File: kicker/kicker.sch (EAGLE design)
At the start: 21 parts, among them T1 NPN_BC817,215, T3 NPN_BC817,215, X1 JST-XH-06-PIN-LONG-PAD

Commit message: Updating designs
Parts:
- added T2, T4: NPN_BC817,215, rhoban:NPN_BC817,215
- R1: value 1K -> 3K; FARNELL 2446904 -> 2446965
- R4: value 1K -> 3K
- U$1, U$11: FARNELL 1095012 -> 2429705
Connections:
- new net N$5: R1.1, T2.B
- new net N$6: R4.1, T4.B
- net GND: now also T2.E, T4.E
- net KICK1: now also R1.2; no longer R1.1
- net N$1: now also T2.C; no longer R1.2
- net N$3: now also T4.C; no longer R4.1
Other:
- moved on the sheet: R1, R2, R32, R33, R34, R35, R4, SOLENOID2, T3, X1-1, X1-2, X1-3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

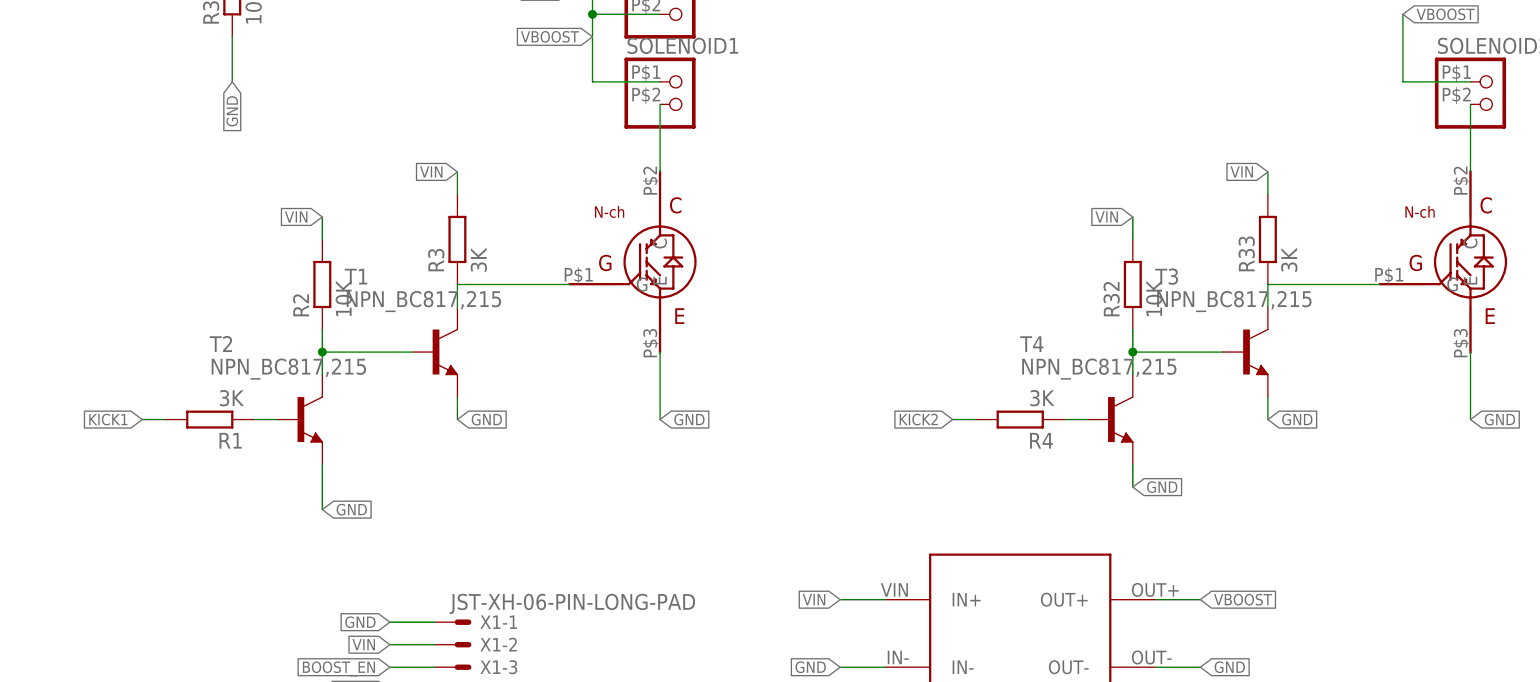
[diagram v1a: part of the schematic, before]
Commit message: Adding resistor on big mos gates
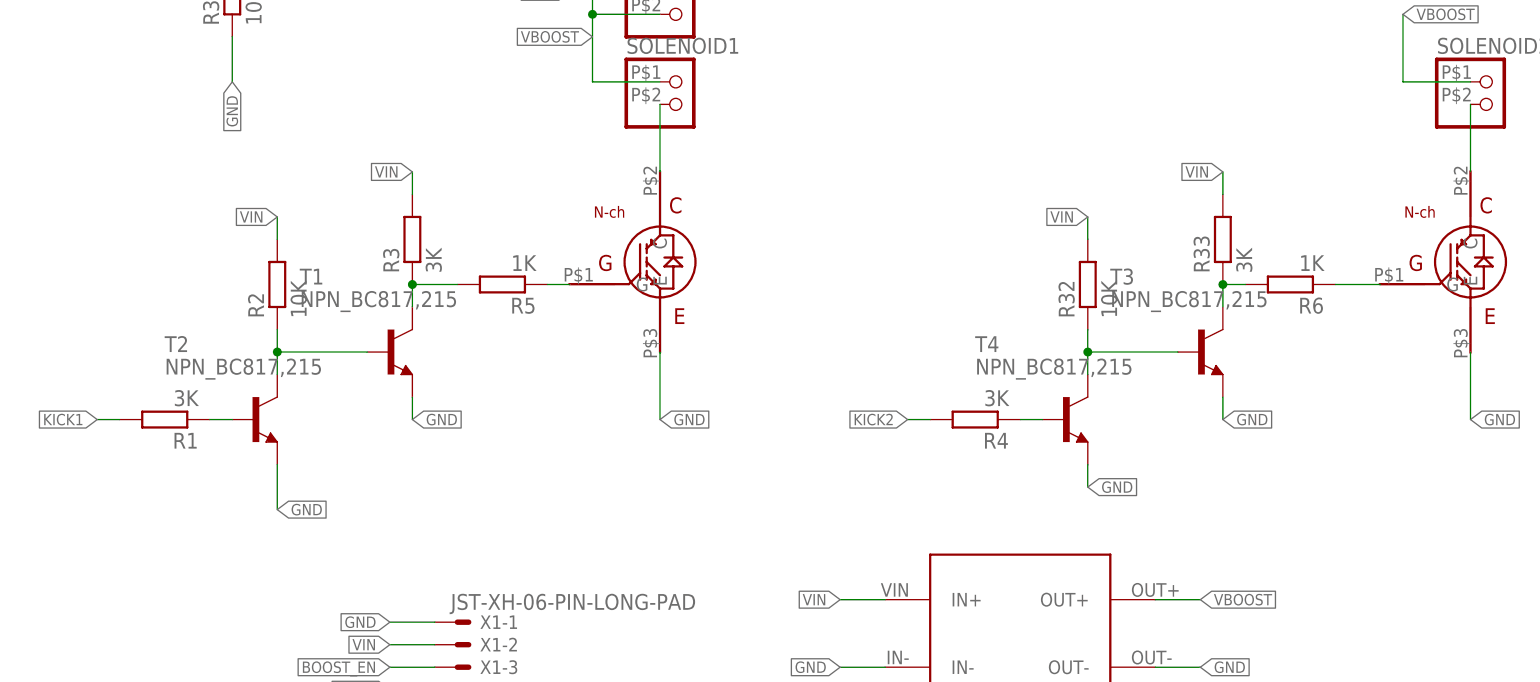
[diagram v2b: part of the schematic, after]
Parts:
- added R5, R6: 1K, rhoban:RESISTANCE-R0805
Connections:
- new net N$7: R5.1, U$1.G
- new net N$8: R6.1, U$11.G
- net N$35: now also R6.2; no longer U$11.G
- net N$4: now also R5.2; no longer U$1.G
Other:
- moved on the sheet: R1, R2, R3, R32, R33, R4, T1, T2, T3, T4

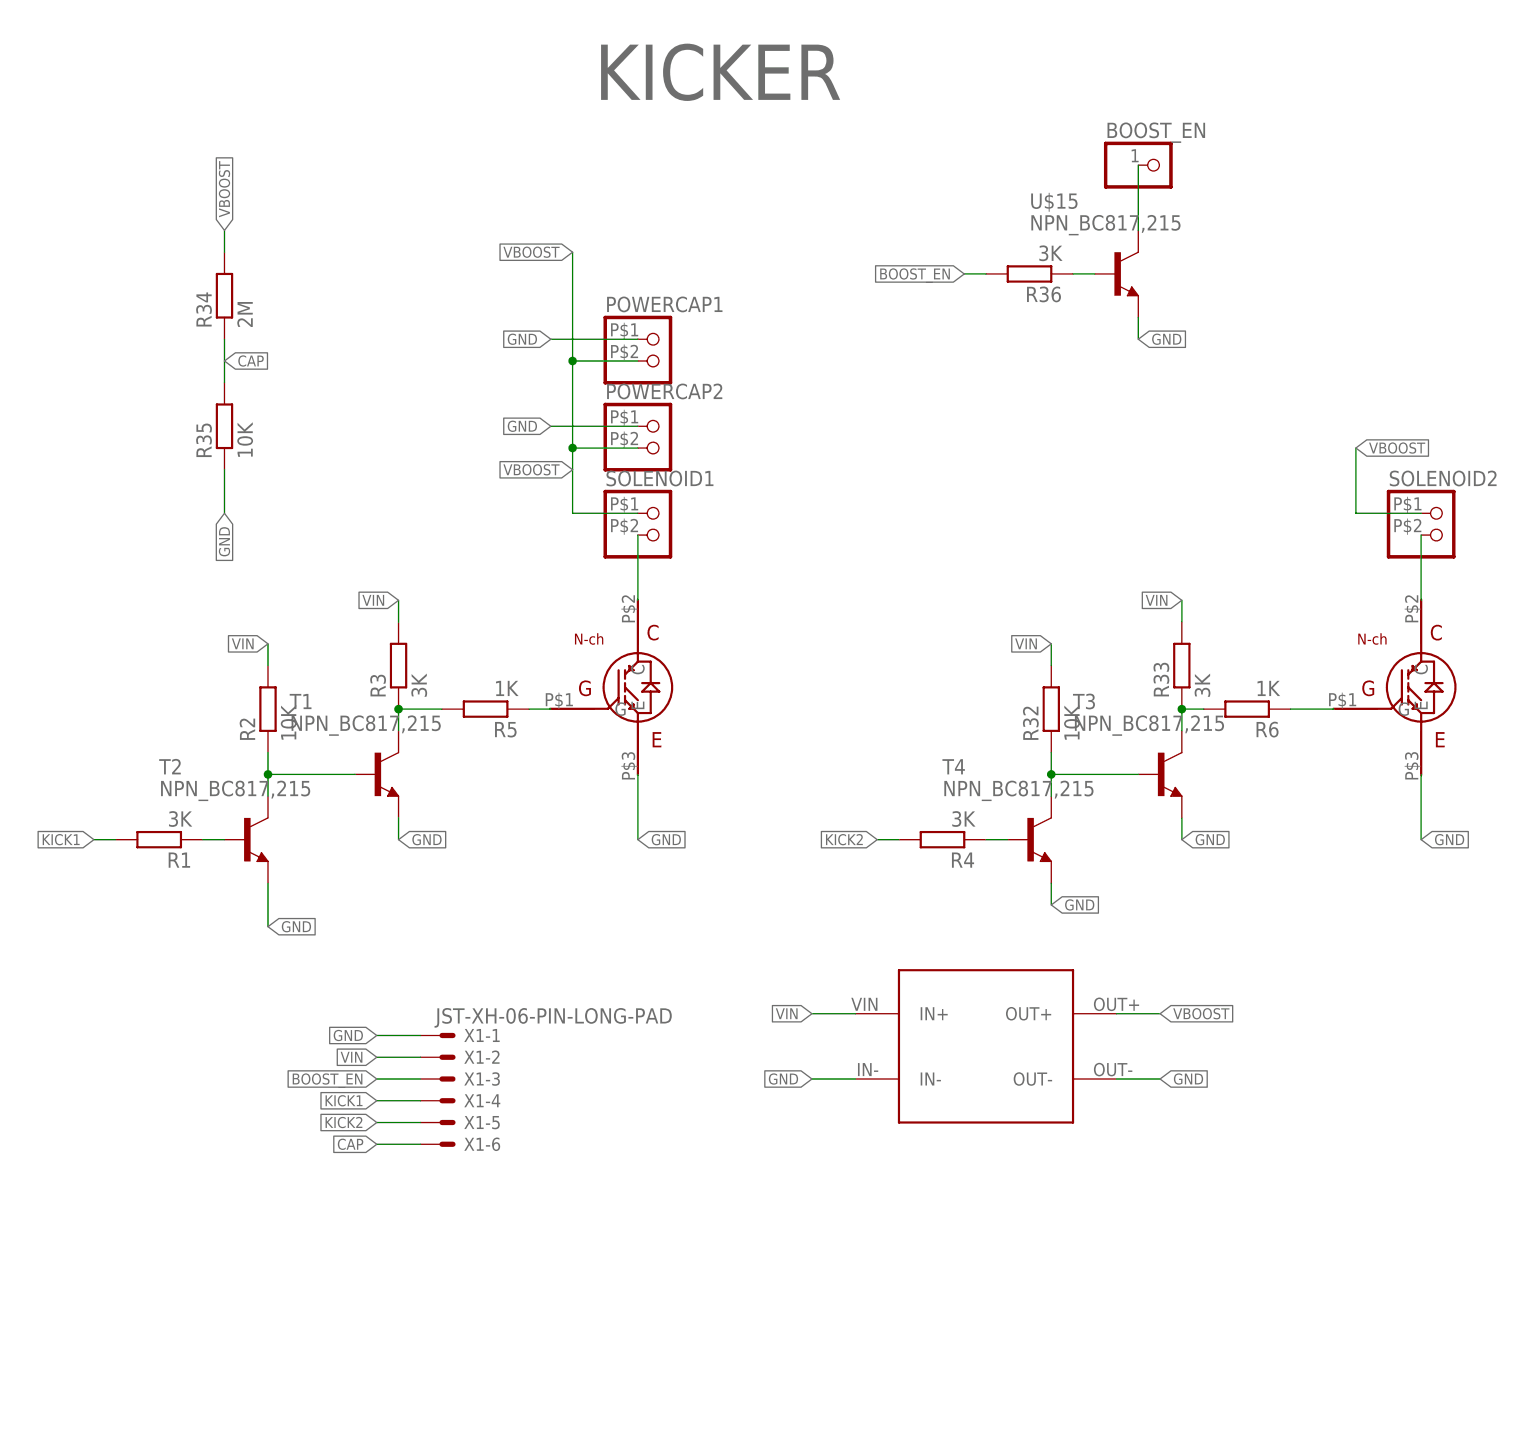
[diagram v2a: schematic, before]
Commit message: 1K on grid
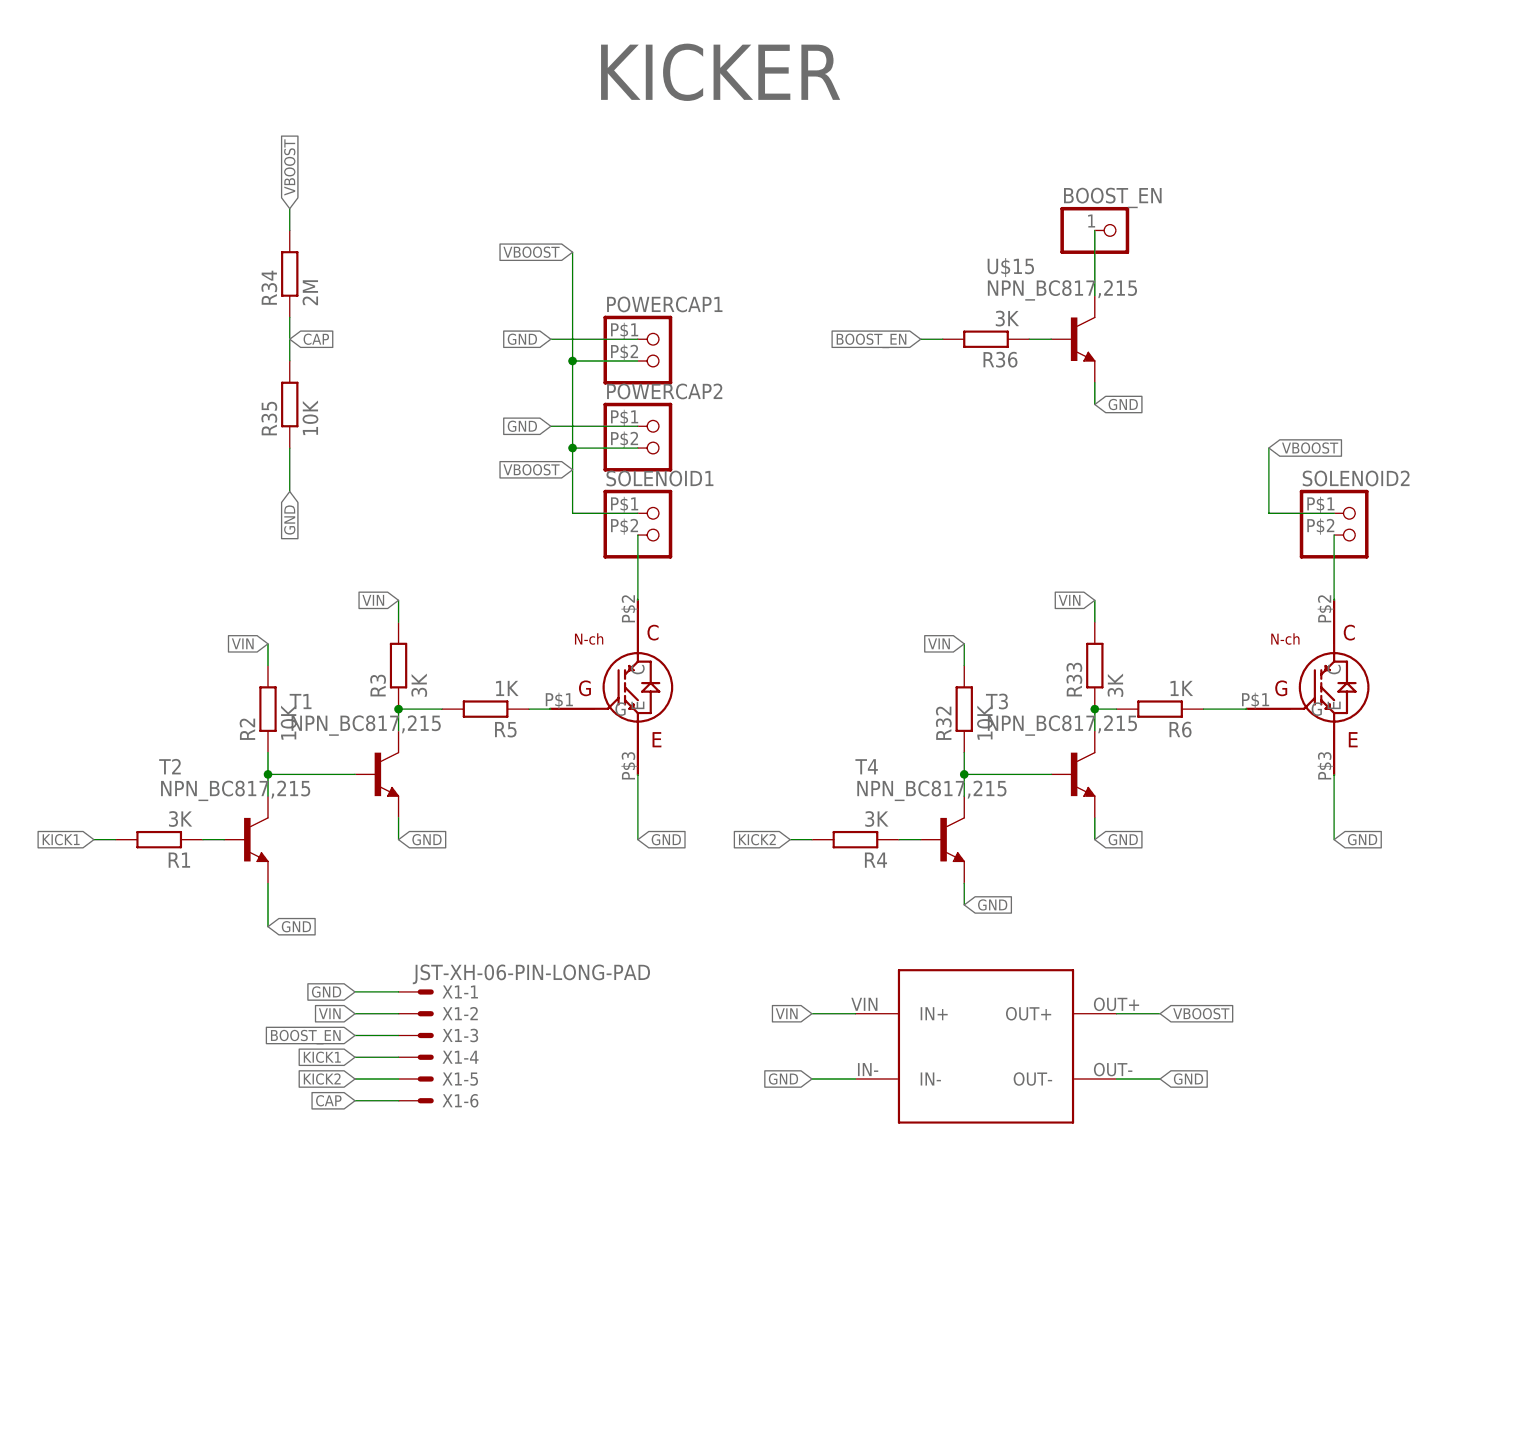
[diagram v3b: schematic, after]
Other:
- moved on the sheet: BOOST_EN, R32, R33, R34, R35, R36, R4, R6, SOLENOID2, T3, T4, U$15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

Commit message: Updating BOMs and ATTRs
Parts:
- X1: FARNELL (none) -> -
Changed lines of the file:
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@@
 <attribute name="FARNELL" value="2446965"/>
 </part>
-<part name="X1" library="Rembrandt Electronics - JST XH Connectors v1-0" deviceset="JST-XH-06-PIN" device="-LONG-PAD"/>
+<part name="X1" library="Rembrandt Electronics - JST XH Connectors v1-0" deviceset="JST-XH-06-PIN" device="-LONG-PAD">
+<attribute name="FARNELL" value="-"/>
+</part>
 <part name="U$5" library="rhoban" deviceset="BOOSTER" device="">
 <attribute name="FARNELL" value="-"/>
@@
 <attribute name="FARNELL" x="33.02" y="63.5" size="1.778" layer="96" rot="R180" display="off"/>
 </instance>
-<instance part="X1" gate="-1" x="-33.02" y="-12.7"/>
+<instance part="X1" gate="-1" x="-33.02" y="-12.7">
+<attribute name="FARNELL" x="-33.02" y="-12.7" size="1.778" layer="96" display="off"/>
+</instance>
 <instance part="X1" gate="-2" x="-33.02" y="-15.24"/>
 <instance part="X1" gate="-3" x="-33.02" y="-17.78"/>
